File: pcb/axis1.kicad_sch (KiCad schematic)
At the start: 7 parts, among them J11 Mini v1.0 / 15-hole socket, J21 MOTOR PHASES male 1x3, J31 ENCODER breakout FEMALE 1x6

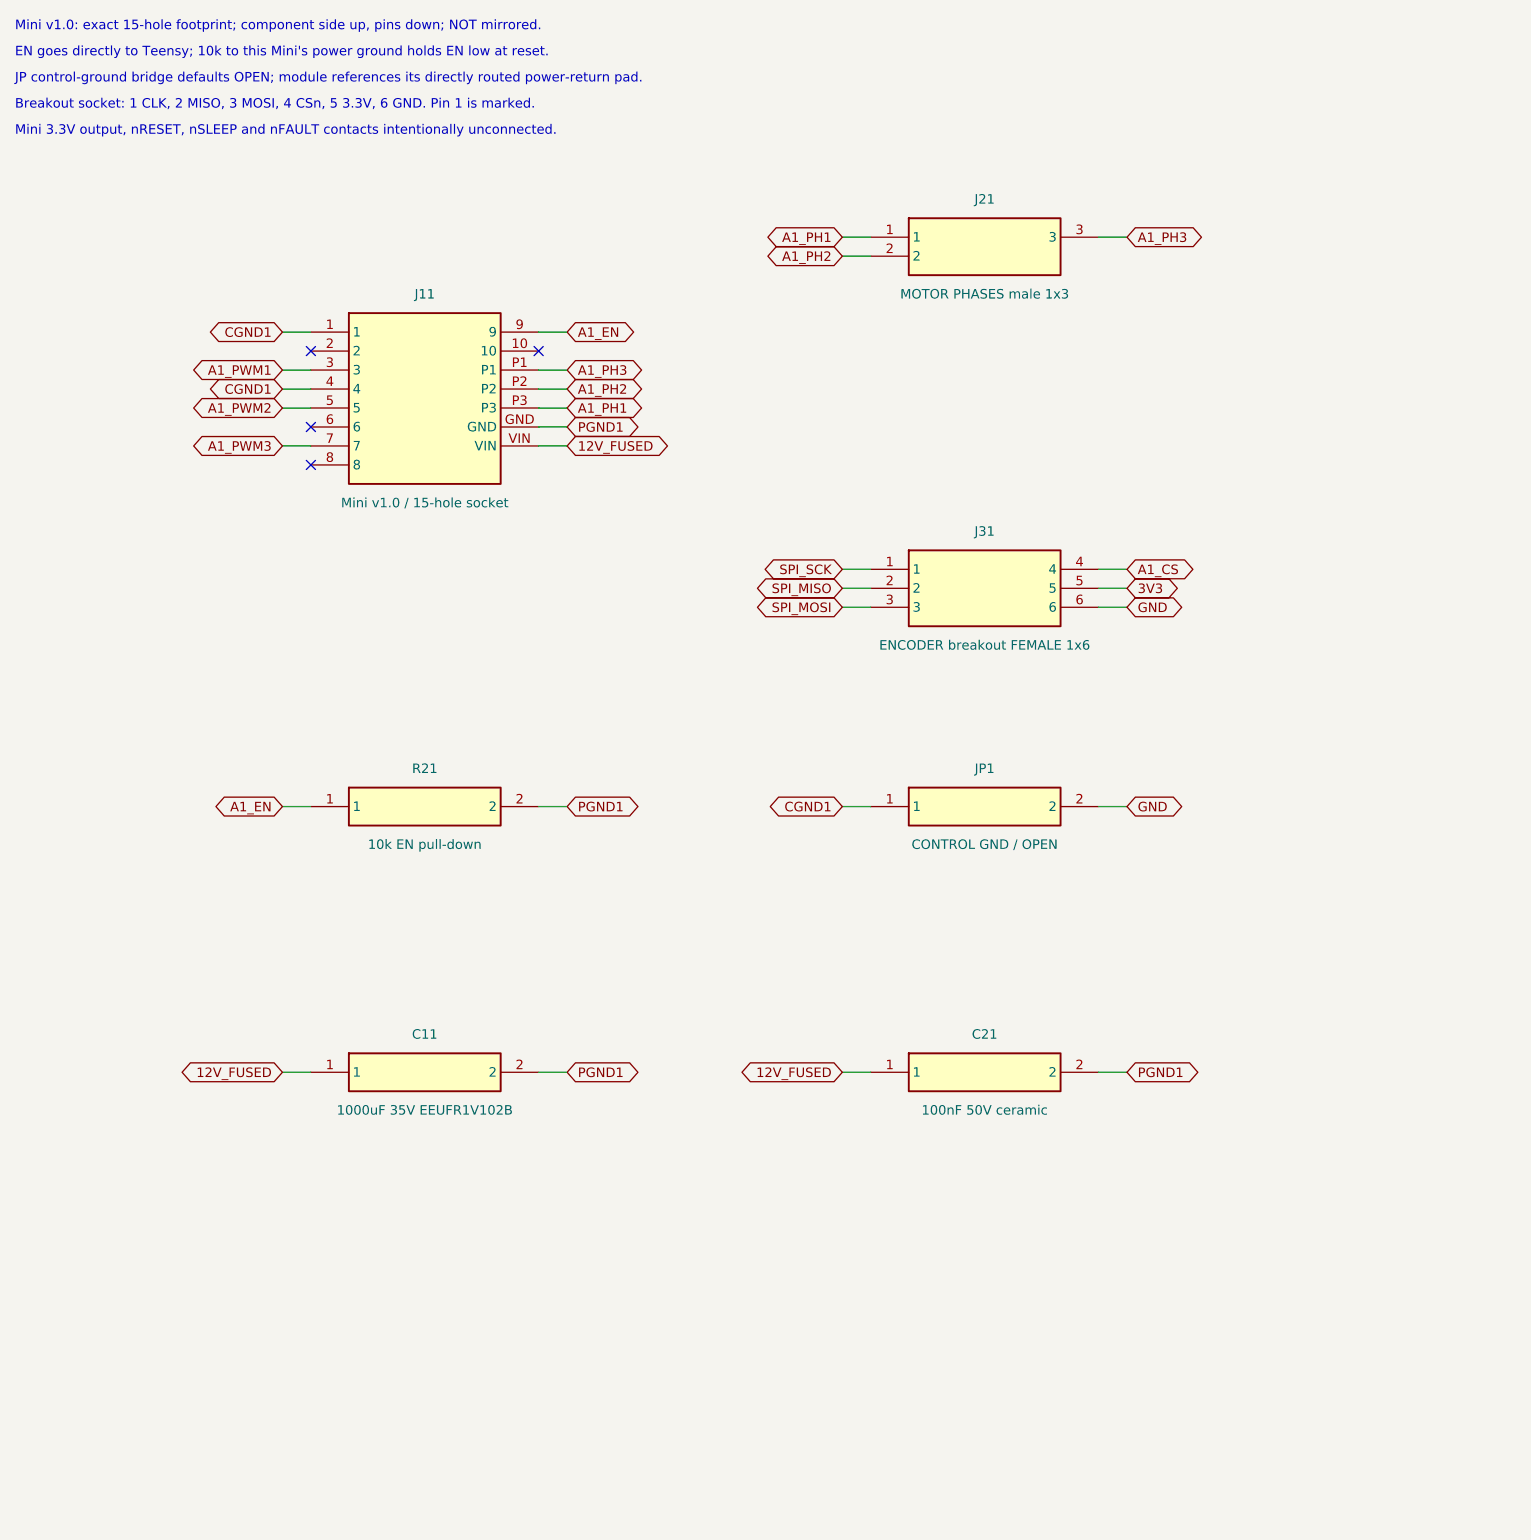
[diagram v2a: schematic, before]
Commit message: feat: relayout carrier with edge connectors and hardware kill
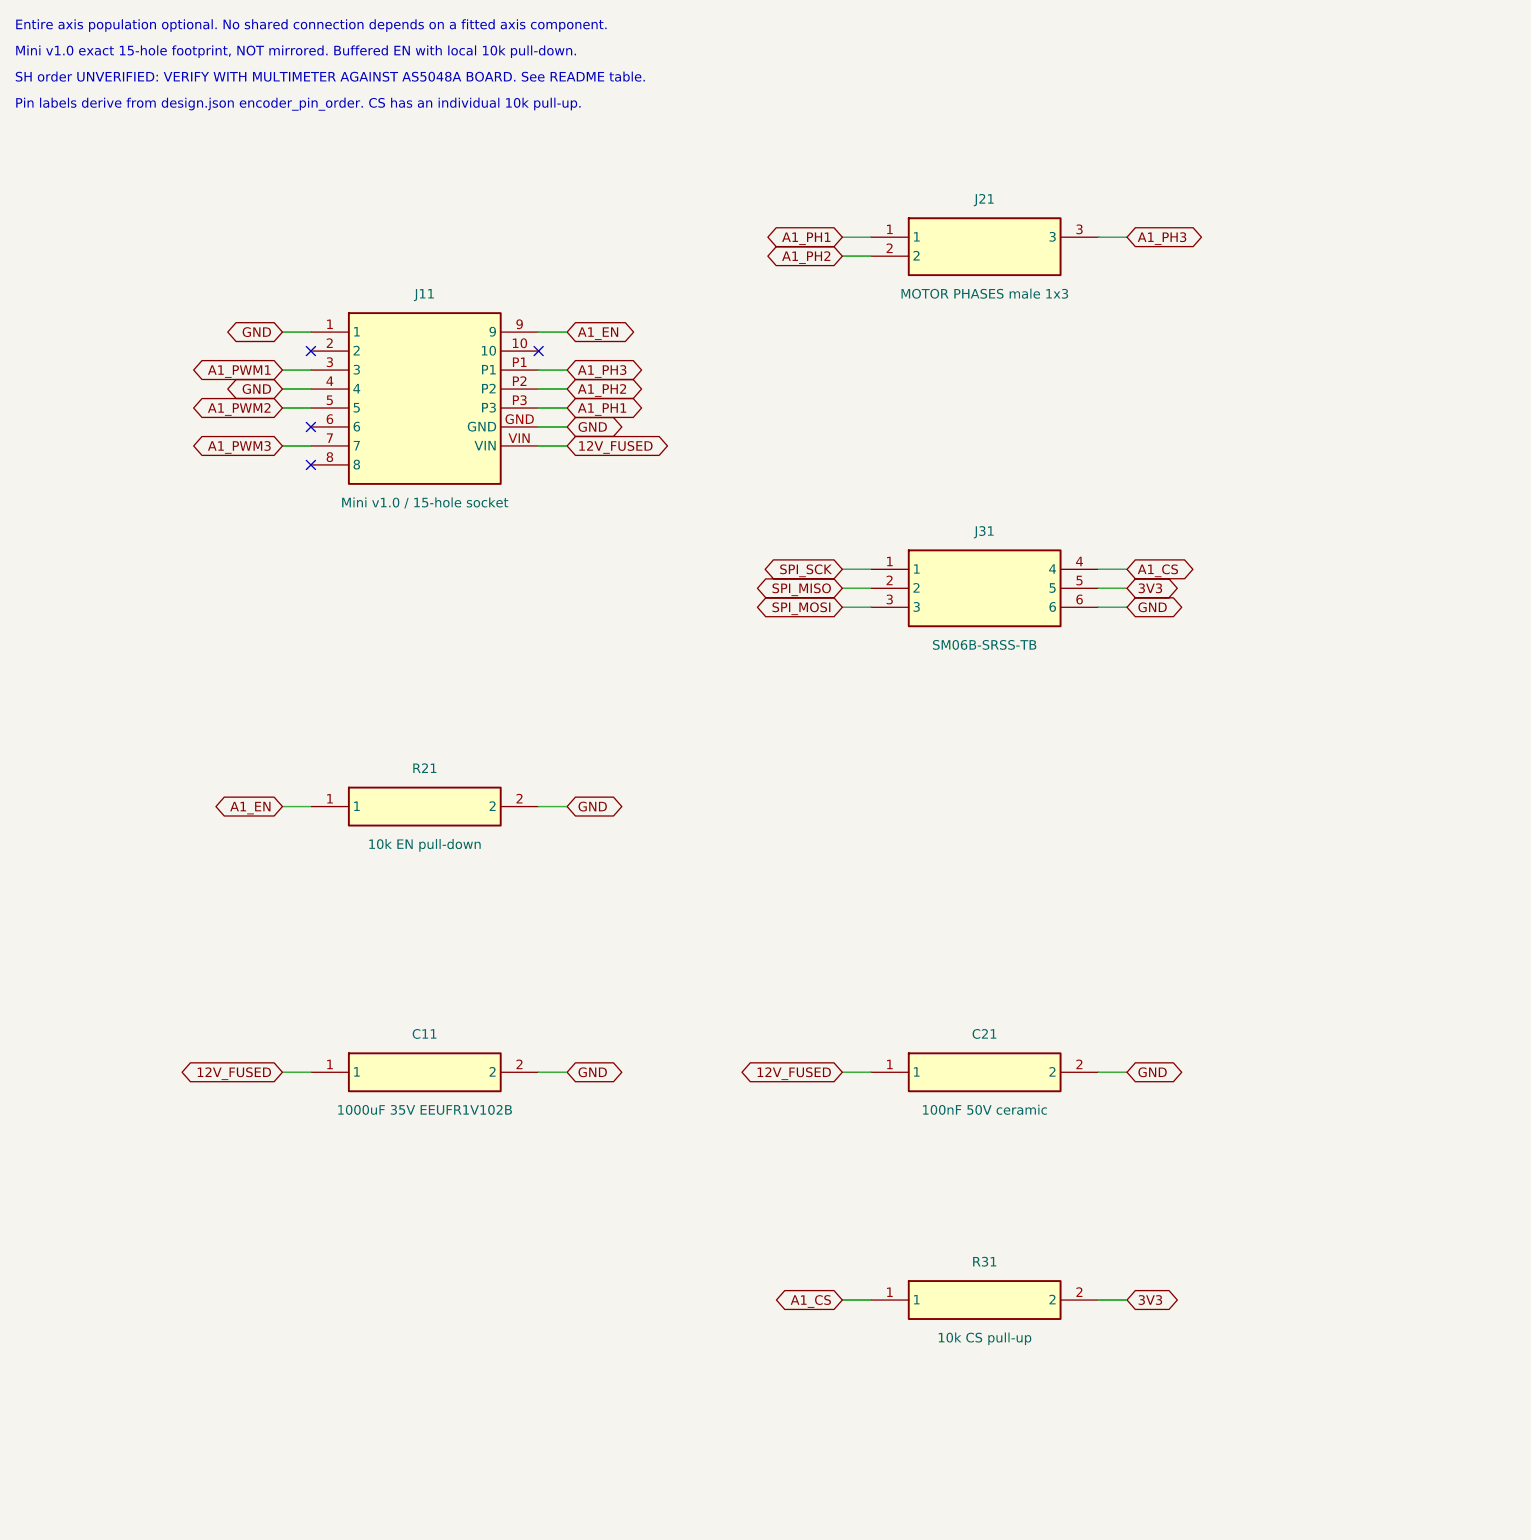
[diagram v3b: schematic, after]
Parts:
- removed JP1: CONTROL GND / OPEN, TrueSkate:GroundBridge_THT, symbol TrueSkate:JP1
- added R31: 10k CS pull-up, TrueSkate:Edge_R_Axial_DIN0207_L6.3mm_D2.5mm_P7.62mm_Horizontal, symbol TrueSkate:R31
- C11: footprint Capacitor_THT:CP_Radial_D12.5mm_P5.00mm -> TrueSkate:Edge_CP_Radial_D12.5mm_P5.00mm
- C21: footprint Capacitor_THT:C_Disc_D5.0mm_W2.5mm_P5.00mm -> TrueSkate:Edge_C_Disc_D5.0mm_W2.5mm_P5.00mm
- J21: footprint Connector_PinHeader_2.54mm:PinHeader_1x03_P2.54mm_Vertical -> TrueSkate:Edge_PinHeader_1x03_P2.54mm_Vertical
- J31: value ENCODER breakout FEMALE 1x6 -> SM06B-SRSS-TB; footprint Connector_PinSocket_2.54mm:PinSocket_1x06_P2.54mm_Vertical -> TrueSkate:Edge_JST_SH_SM06B-SRSS-TB_1x06-1MP_P1.00mm_Horizontal
- R21: footprint Resistor_THT:R_Axial_DIN0207_L6.3mm_D2.5mm_P7.62mm_Horizontal -> TrueSkate:Edge_R_Axial_DIN0207_L6.3mm_D2.5mm_P7.62mm_Horizontal
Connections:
- net CGND1 is gone; now on net GND: J11.1, J11.4
- net PGND1 is gone; now on net GND: C11.2, C21.2, J11.GND, R21.2
- net 3V3: now also R31.2
- net A1_CS: now also R31.1
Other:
- note added: "Entire axis population optional. No shared connection depends on a fitted axis component."
- note added: "Mini v1.0 exact 15-hole footprint, NOT mirrored. Buffered EN with local 10k pull-down."
- note added: "Pin labels derive from design.json encoder_pin_order. CS has an individual 10k pull-up."
- note added: "SH order UNVERIFIED: VERIFY WITH MULTIMETER AGAINST AS5048A BOARD. See README table."
- note removed: "Breakout socket: 1 CLK, 2 MISO, 3 MOSI, 4 CSn, 5 3.3V, 6 GND. Pin 1 is marked."
- note removed: "EN goes directly to Teensy; 10k to this Mini's power ground holds EN low at reset."
- note removed: "JP control-ground bridge defaults OPEN; module references its directly routed power-return pad."
- note removed: "Mini 3.3V output, nRESET, nSLEEP and nFAULT contacts intentionally unconnected."
- note removed: "Mini v1.0: exact 15-hole footprint; component side up, pins down; NOT mirrored."
